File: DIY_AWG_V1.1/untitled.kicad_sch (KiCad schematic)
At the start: 56 parts, among them U1 ADP7118ARDZ, U16 TPS7A4701RGWR, U17 TPS7A4701RGWR, U2 ADP7118ARDZ, U3 TPS7A3301RGWR, U4 ADP7118ARDZ, U5 ADP7182ACPZN-R7

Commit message: Updated STM32_MCU schematic
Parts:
- added C17, C86: 47u, symbol Device:C
- added C21: 2.2u, symbol Device:C
- added C33, C34: 22u, symbol Device:C_Polarized
- added C85: 10n, symbol Device:C
- added L15: 0.33u, symbol Device:L
- added R13, R14: 400m, symbol Device:R
- added R15: 332k, symbol Device:R
- added R48: 102k, symbol Device:R
- added TP33: TestPoint, symbol Connector:TestPoint
- added U10: AMS1117-3.3, easyeda2kicad:SOT-223-3_L6.5-W3.4-P2.30-LS7.0-BR, symbol easyeda2kicad:AMS1117-3.3
- added U6: TPS7A3301RGWR, easyeda2kicad:VQFN-20_L5.0-W5.0-P0.65-TL-EP, symbol easyeda2kicad:TPS7A3301RGWR
- C19: value 1u -> 2.2u
- R10: value 215 -> 215k
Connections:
- net +5V: now also C33.1, U10.3 (VIN)
- net -5.0VA: now also C85.1, C86.1, R15.1, TP33.1, U6.1 (OUT), U6.20 (OUT)
- net -VSW12V0: now also L15.1, R13.1, R14.1
- net GND: now also C17.2, C21.2, C33.2, C34.2, C86.2, R48.2, U10.1 (GND), U6.21 (EPAD), U6.7 (GND)
- net at C16.1, L14.2, U3.13 (EN)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: now also R13.2
- new net: C85.2, R15.2, R48.1, U6.3 (FB)
- new net: C17.1, L15.2, R14.2, U6.15 (IN), U6.16 (IN)
- new net: C21.1, U6.14 (NR/SS)
- new net +3V3: C34.1, U10.2 (VOUT), U10.4 (VOUT)
- no-connect marks 31 -> 43
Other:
- note added: "-VDDA for LMH6505 (Using TPS7A3301RGWR 2)"
- note added: "4.7nF MLCC (3): 04023C472KAT2A 2.2uF MLCC (10): TAJB226K016RNJ 3.3uF MLCC (4): CL21B335KAFNFNE 22uF MLCC (4): 47uF MLCC (6):"
- note added: "TAJB226K016RNJ"
- note added: "VDD for STM32, AD9834 (Using AMS1117 1)"
- note removed: "2.2uF MLCC (10): TAJB226K016RNJ 4.7nF MLCC (5): 04023C472KAT2A 3.3uF MLCC (4): CL21B335KAFNFNE"
- note removed: "WARNING: ADP7118 and ADP7182 might saturate supplying current for THS3091 Fix: Change to TPS7A4701 and TPS7A3301RGWR"
- moved on the sheet: C10, C11, C15, C16, C18, C19, C2, C20, C4, C6, C77, C78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

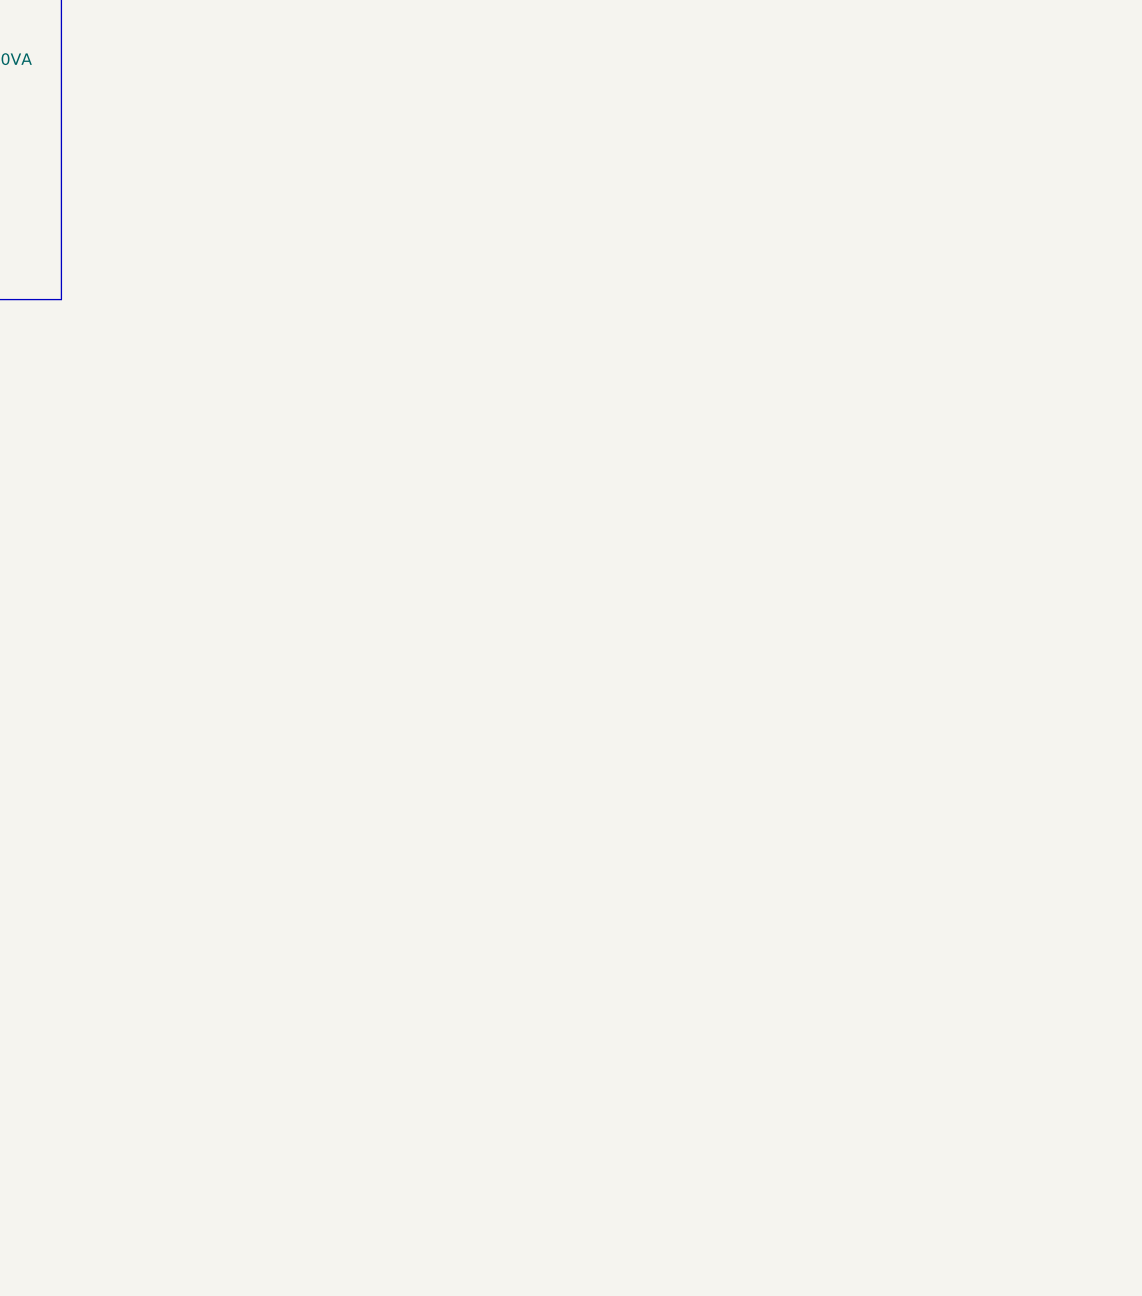
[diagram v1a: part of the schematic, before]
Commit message: Updated power_supply schematic
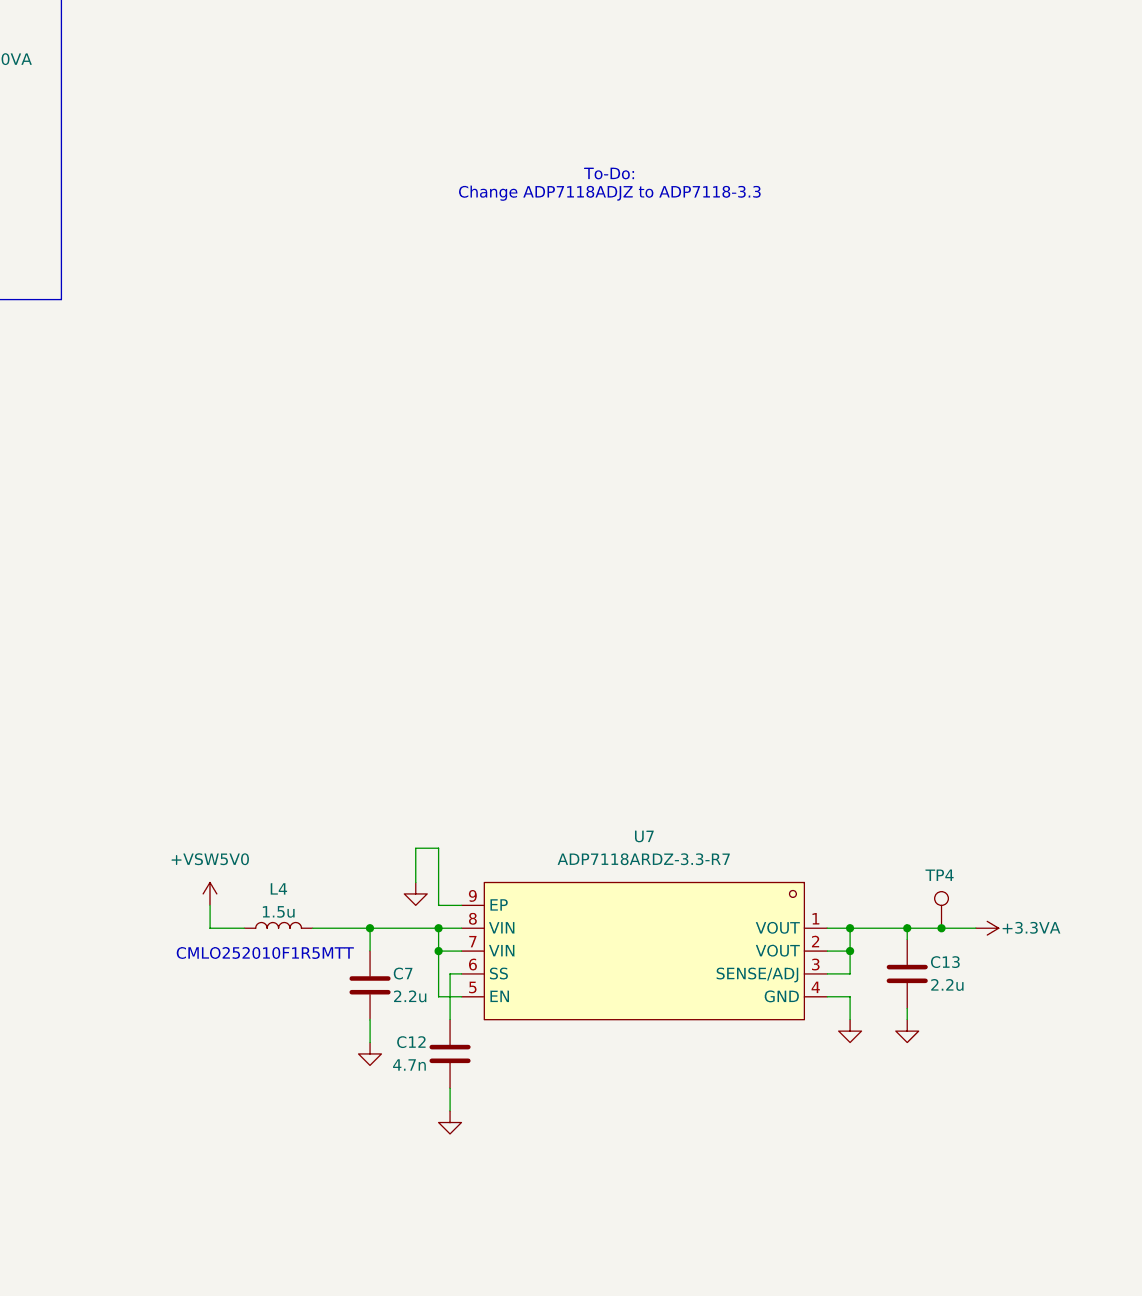
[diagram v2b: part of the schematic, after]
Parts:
- added C12: 4.7n, symbol Device:C
- added C13, C7: 2.2u, symbol Device:C
- added L4: 1.5u, symbol Device:L
- added TP4: TestPoint, symbol Connector:TestPoint
- added U7: ADP7118ARDZ-3.3-R7, easyeda2kicad:SOIC-8_L4.9-W3.9-P1.27-LS6.0-BL-EP2.3, symbol easyeda2kicad:ADP7118ARDZ-3.3-R7
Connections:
- net +3.3VA: now also C13.1, TP4.1, U7.1 (VOUT), U7.2 (VOUT), U7.3 (SENSE/ADJ)
- net +5V: now also L4.1
- net GND: now also C12.2, C13.2, C7.2, U7.4 (GND), U7.9 (EP)
- new net: C7.1, L4.2, U7.5 (EN), U7.7 (VIN), U7.8 (VIN)
- new net: C12.1, U7.6 (SS)
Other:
- note added: "CMLO252010F1R5MTT"
- note added: "To-Do: Change ADP7118ADJZ to ADP7118-3.3"

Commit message: Updated power_supply schematics
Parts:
- removed C1, C10, C11, C2, C4, C9: 2.2u, symbol Device:C
- removed C5, C6: 4.7n, symbol Device:C
- removed L1, L2, L3: 1.5u, symbol Device:L
- removed R1, R3, R7: 4k, symbol Device:R
- removed R2, R4, R8: 15k, symbol Device:R
- removed TP1, TP2, TP3: TestPoint, symbol Connector:TestPoint
- removed U1, U2, U4: ADP7118ARDZ, easyeda2kicad:SOIC-8_L4.9-W3.9-P1.27-LS6.0-BL-EP2.3, symbol easyeda2kicad:ADP7118ARDZ
- added C14: 4.7n, symbol Device:C
- added C87: 2.2u, symbol Device:C
- added L5: 1.5u, symbol Device:L
- added R49, R50: 400m, symbol Device:R
- added TP5: TestPoint, symbol Connector:TestPoint
- added U18: ADP7118ARDZ-3.3-R7, easyeda2kicad:SOIC-8_L4.9-W3.9-P1.27-LS6.0-BL-EP2.3, symbol easyeda2kicad:ADP7118ARDZ-3.3-R7
- C8: value 4.7n -> 2.2u
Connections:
- net +3.3VA: now also C87.1, TP5.1, U18.1 (VOUT), U18.2 (VOUT), U18.3 (SENSE/ADJ)
- net +5V: now also L5.1, R49.1, R50.1
- net GND: now also C14.2, C87.2, U18.4 (GND), U18.9 (EP)
- net at C7.1, L4.2, U7.5 (EN)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: now also R49.2
- net at C8.1: now also L5.2, R50.2, U18.5 (EN), U18.7 (VIN), U18.8 (VIN)
- new net: C14.1, U18.6 (SS)
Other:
- note added: "4.7nF MLCC (3): 04023C472KAT2A 2.2uF MLCC (10): CL21B335KAFNFNE 3.3uF MLCC (4): CL21B335KAFNFNE 22uF MLCC (4): 47uF MLCC (6):"
- note added: "Question: 1. Is it better to share the LDOs for AD9834 with ADG704, or AD9834 with STM32?"
- note added: "VDDA for STM32, AD9834 (Using ADP7118 2)"
- note removed: "4.7nF MLCC (3): 04023C472KAT2A 2.2uF MLCC (10): TAJB226K016RNJ 3.3uF MLCC (4): CL21B335KAFNFNE 22uF MLCC (4): 47uF MLCC (6):"
- note removed: "APCA000606451R5T00"
- note removed: "VDDA for AD9834 (Using ADP7118 2)"
- note removed: "VDDA for STM32 (Using ADP7118 2)"
- moved on the sheet: C12, C13, C16, C19, C33, C34, C7, C77, C78, C79, C83, C84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

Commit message: Updated power_supply schematic
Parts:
- removed C15, C18: 3.3u, symbol Device:C
- removed C20: 100n, symbol Device:C
- removed L6: 4.7u, symbol Device:L
- removed R11: 30.9k, symbol Device:R
- removed R12: 10k, symbol Device:R
- removed R16: 3k, symbol Device:R
- removed TP6: TestPoint, symbol Connector:TestPoint
- removed U5: ADP7182ACPZN-R7, easyeda2kicad:LFCSP-6_L2.0-W2.0-P0.65-TL-EP, symbol easyeda2kicad:ADP7182ACPZN-R7
- added C100, C88, C92, C96: 22u, symbol Device:C
- added C101, C102, C103, C89, C90, C91, C93, C94, C95, C97, C98, C99: 47u, symbol Device:C
- C16, C17: value 47u -> 22u
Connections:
- net +10.0VA: now also C89.1, C90.1, C91.1
- net +5.0VA: now also C97.1, C98.1, C99.1
- net -10.0VA: now also C93.1, C94.1, C95.1
- net -5.0VA: now also C101.1, C102.1, C103.1
- net GND: now also C100.2, C101.2, C102.2, C103.2, C88.2, C89.2, C90.2, C91.2, C92.2, C93.2, C94.2, C95.2, C96.2, C97.2, C98.2, C99.2
- net at C16.1, L14.2, R13.2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: now also C92.1
- net at C17.1, L15.2, R14.2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: now also C100.1
- net at C80.1, L13.2, R6.2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: now also C96.1
- net at C77.1, L12.2, R5.2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: now also C88.1
- no-connect marks 43 -> 42
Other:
- note added: "4.7nF MLCC (2): 04023C472KAT2A (2) 2.2uF MLCC (8): CL21B335KAFNFNE (8) 22uF MLCC (4): GRM31CR61E476ME44L (8) 47uF MLCC (4): GRM31CR61E476ME44L (16) 22uF Tantalum Cap (2): TAJB226K016RNJ (2) 1.5uH Inductor (2): CMLO252010F1R5MTT (2) 0.47uH Inductor (2): MNR252010TR47NT (2) 0.33uH Inductor (2): CMLO252010FR33MTT (2)"
- note added: "CMLO252010FR33MTT"
- note added: "MNR252010TR47NT"
- note added: "Place 2 GRM31CR61E476ME44L in parallel"
- note added: "Place 4 GRM31CR61E476ME44L in parallel for effective 47uF capacitance"
- note removed: "-12.0V from Buck Converter"
- note removed: "-VDDA for LMH6505 (Using ADP7182 2)"
- note removed: "4.7nF MLCC (3): 04023C472KAT2A 2.2uF MLCC (10): CL21B335KAFNFNE 3.3uF MLCC (4): CL21B335KAFNFNE 22uF MLCC (4): 47uF MLCC (6):"
- note removed: "CMLO252010F4R7MTT"
- note removed: "To-Do: Change ADP7118ADJZ to ADP7118-3.3"
- moved on the sheet: C17, C19, C21, C78, C79, C80, C81, C82, C83, C84, C85, C86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

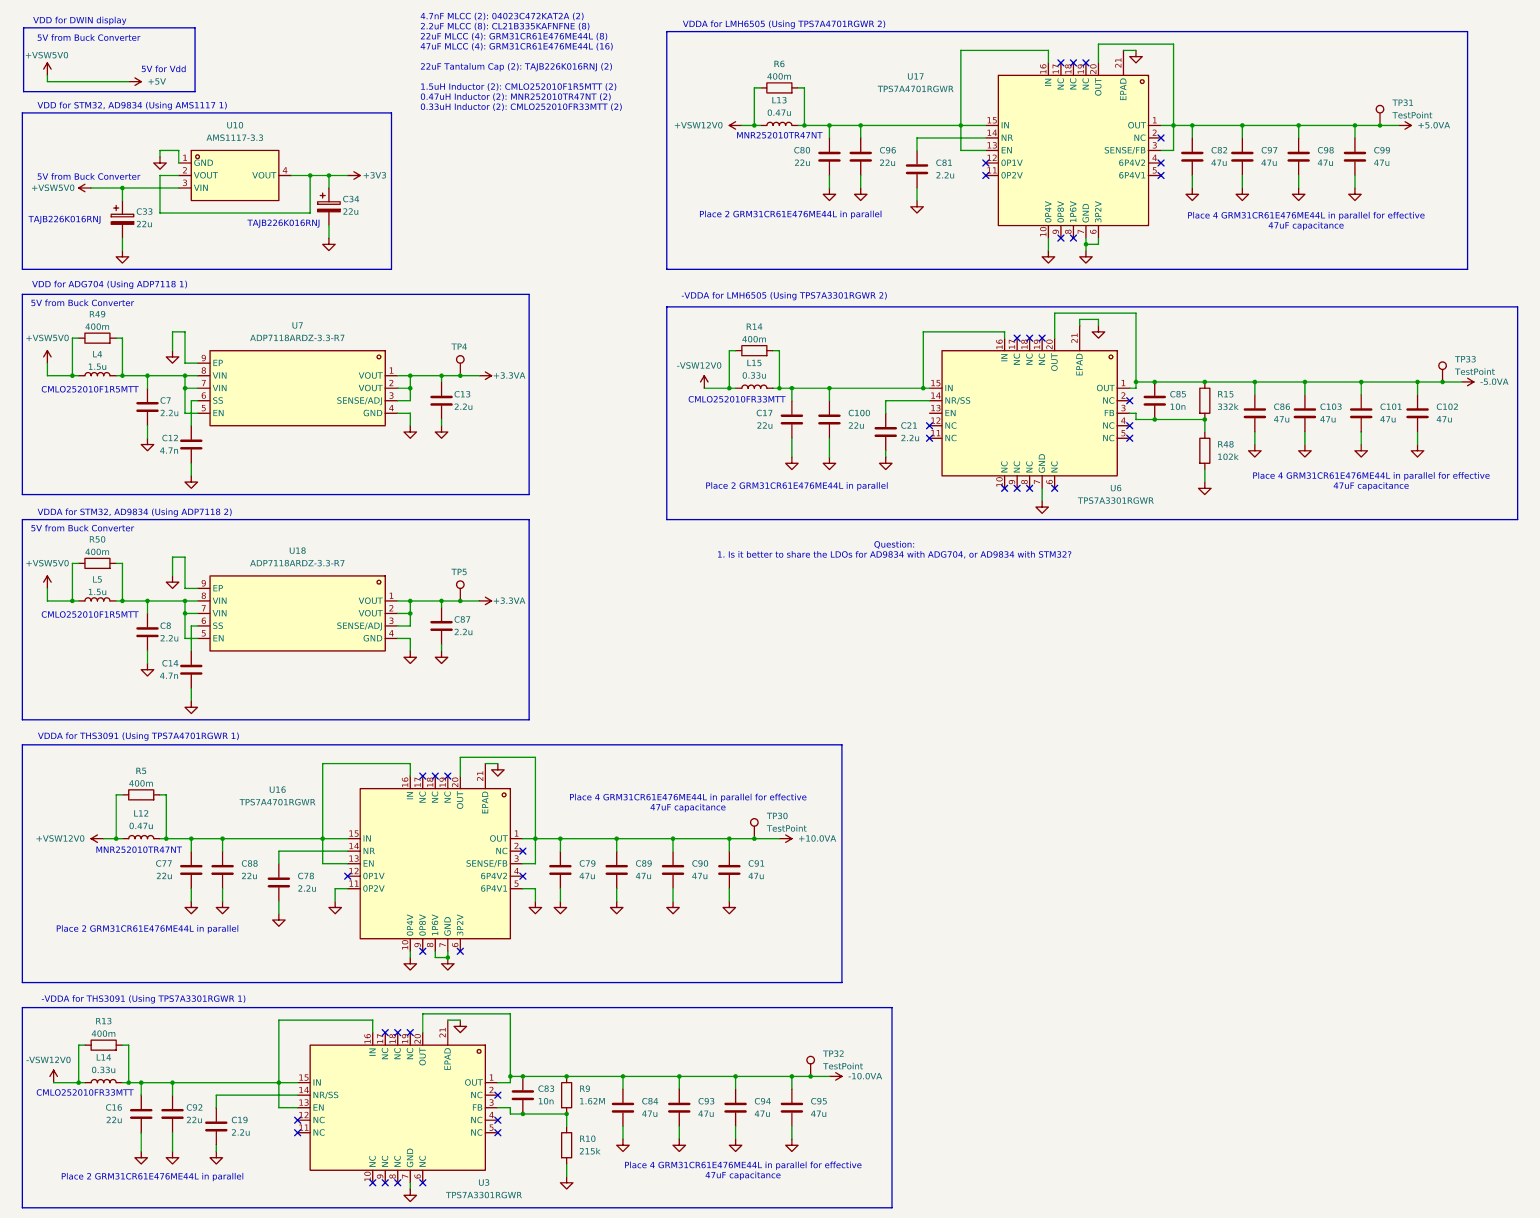
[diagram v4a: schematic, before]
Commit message: Updated power_supply, amplifier schematics
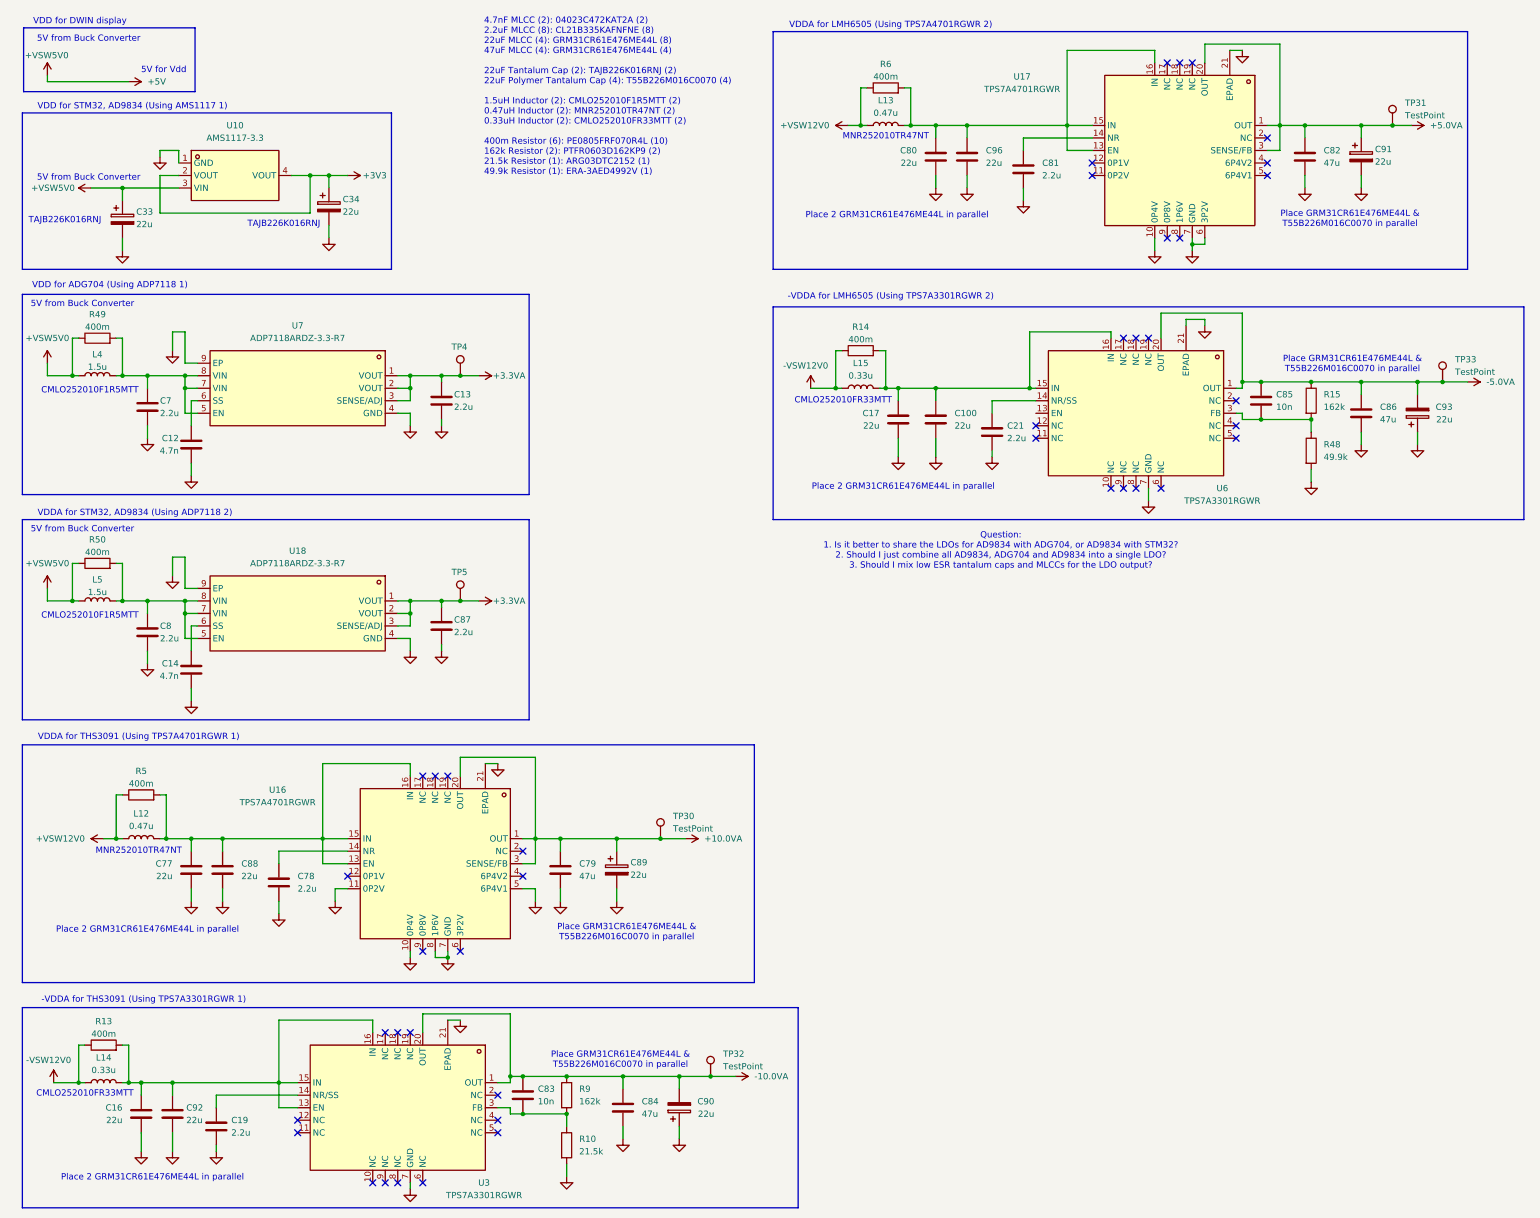
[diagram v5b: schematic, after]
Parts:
- removed C101, C102, C103, C89, C90, C91, C93, C94, C95, C97, C98, C99: 47u, symbol Device:C
- added C89, C90, C91, C93: 22u, symbol Device:C_Polarized
- R10: value 215k -> 21.5k
- R15: value 332k -> 162k
- R48: value 102k -> 49.9k
- R9: value 1.62M -> 162k
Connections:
- net +10.0VA: now also C89.1
- net +5.0VA: now also C91.1
- net -10.0VA: now also C90.2
- net -5.0VA: now also C93.2
- net GND: now also C89.2, C90.1, C91.2, C93.1
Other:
- note added: "4.7nF MLCC (2): 04023C472KAT2A (2) 2.2uF MLCC (8): CL21B335KAFNFNE (8) 22uF MLCC (4): GRM31CR61E476ME44L (8) 47uF MLCC (4): GRM31CR61E476ME44L (4) 22uF Tantalum Cap (2): TAJB226K016RNJ (2) 22uF Polymer Tantalum Cap (4): T55B226M016C0070 (4) 1.5uH Inductor (2): CMLO252010F1R5MTT (2) 0.47uH Inductor (2): MNR252010TR47NT (2) 0.33uH Inductor (2): CMLO252010FR33MTT (2) 400m Resistor (6): PE0805FRF070R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"
- note added: "Place GRM31CR61E476ME44L & T55B226M016C0070 in parallel"
- note added: "Question: 1. Is it better to share the LDOs for AD9834 with ADG704, or AD9834 with STM32? 2. Should I just combine all AD9834, ADG704 and AD9834 into a single LDO? 3. Should I mix low ESR tantalum caps and MLCCs for the LDO output?"
- note removed: "4.7nF MLCC (2): 04023C472KAT2A (2) 2.2uF MLCC (8): CL21B335KAFNFNE (8) 22uF MLCC (4): GRM31CR61E476ME44L (8) 47uF MLCC (4): GRM31CR61E476ME44L (16) 22uF Tantalum Cap (2): TAJB226K016RNJ (2) 1.5uH Inductor (2): CMLO252010F1R5MTT (2) 0.47uH Inductor (2): MNR252010TR47NT (2) 0.33uH Inductor (2): CMLO252010FR33MTT (2)"
- note removed: "Place 4 GRM31CR61E476ME44L in parallel for effective 47uF capacitance"
- note removed: "Question: 1. Is it better to share the LDOs for AD9834 with ADG704, or AD9834 with STM32?"
- moved on the sheet: C100, C17, C21, C80, C81, C85, C96, L13, L15, R14, R15, R48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
